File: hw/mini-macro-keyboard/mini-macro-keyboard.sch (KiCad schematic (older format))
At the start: 37 parts

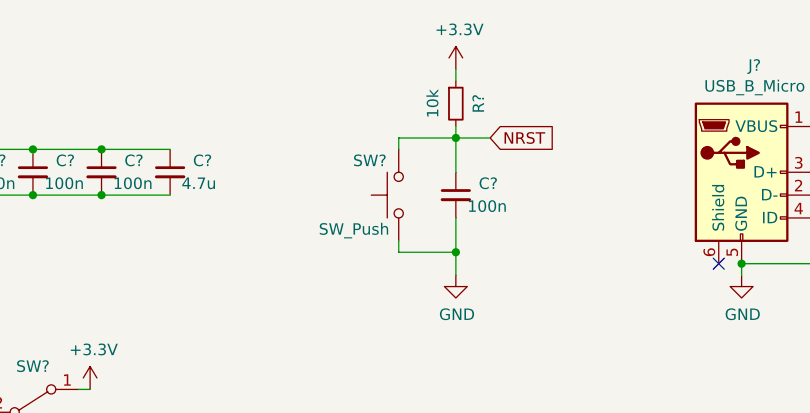
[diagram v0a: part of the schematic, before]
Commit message: style(hw): rename push switch
Signed-off-by: Ivan Kovalenko <s1ckretbox@gmail.com>
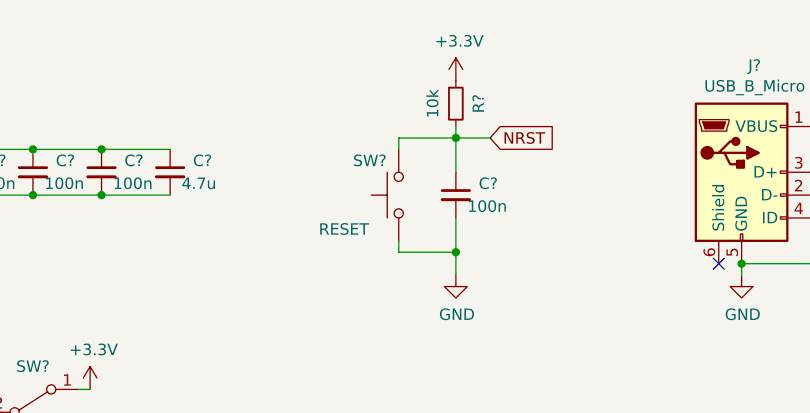
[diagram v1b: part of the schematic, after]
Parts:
- SW?: value SW_Push -> RESET
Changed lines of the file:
@@
 NRST
-Wire Wire Line
-	3750 800  3750 750
 Wire Wire Line
 	3750 1000 3750 1050
@@
 P 3500 1300
 F 0 "SW?" V 3650 1500 50  0000 R CNN
-F 1 "SW_Push" V 3350 1650 50  0000 R CNN
+F 1 "RESET" V 3350 1650 50  0000 R CNN
 F 2 "" H 3500 1500 50  0001 C CNN
 F 3 "~" H 3500 1500 50  0001 C CNN
@@
 L power:+3.3V #PWR?
 U 1 1 5FFB05C0
-P 3750 750
-F 0 "#PWR?" H 3750 600 50  0001 C CNN
-F 1 "+3.3V" H 3765 923 50  0000 C CNN
-F 2 "" H 3750 750 50  0001 C CNN
-F 3 "" H 3750 750 50  0001 C CNN
-	1    3750 750
-	1    0    0    -1
-$EndComp
+P 3750 800
+F 0 "#PWR?" H 3750 650 50  0001 C CNN
+F 1 "+3.3V" H 3765 973 50  0000 C CNN
+F 2 "" H 3750 800 50  0001 C CNN
+F 3 "" H 3750 800 50  0001 C CNN
+	1    3750 800
+	1    0    0    -1
+$EndComp

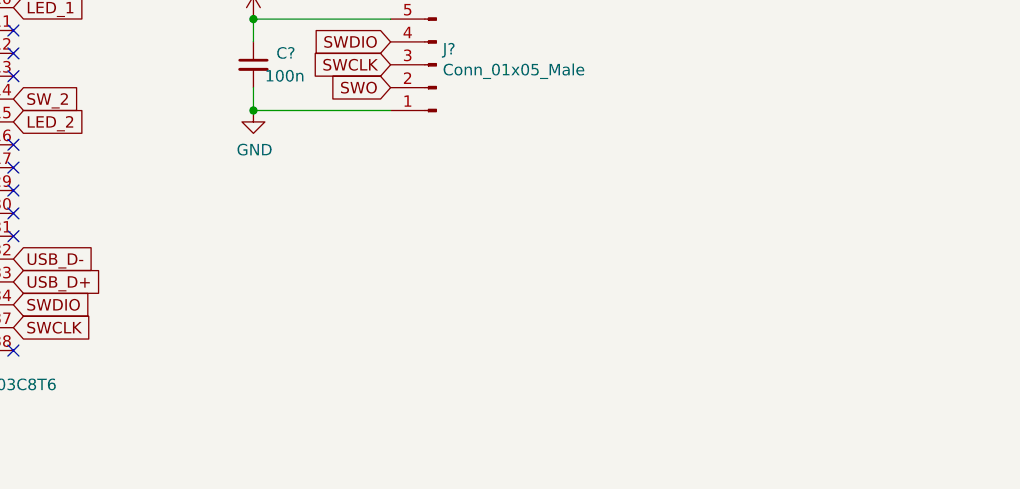
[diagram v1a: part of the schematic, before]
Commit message: feat(hw): add switches
Signed-off-by: Ivan Kovalenko <s1ckretbox@gmail.com>
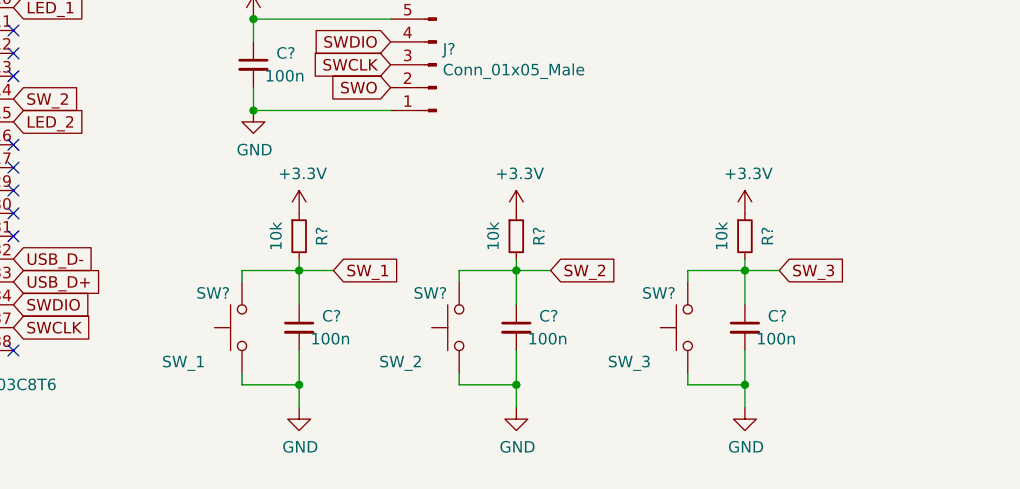
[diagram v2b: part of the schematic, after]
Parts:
- added C? (x3): 100n, symbol Device:C_Small
- added R? (x3): 10k, symbol Device:R_Small
- added SW?: SW_1, symbol Switch:SW_Push
- added SW?: SW_2, symbol Switch:SW_Push
- added SW?: SW_3, symbol Switch:SW_Push
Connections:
- net +3V3: now also R?.1, R?.1, R?.1
- net GND: now also C?.2, C?.2, C?.2, SW?.1, SW?.1, SW?.1
- net SW_1: now also C?.1, R?.2, SW?.2
- net SW_2: now also C?.1, R?.2, SW?.2
- net SW_3: now also C?.1, R?.2, SW?.2
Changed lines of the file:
@@
 	1    0    0    -1
 $EndComp
+$Comp
+L Device:C_Small C?
+U 1 1 5FFBA63C
+P 3750 7050
+F 0 "C?" H 3850 7100 50  0000 L CNN
+F 1 "100n" H 3800 7000 50  0000 L CNN
+F 2 "" H 3750 7050 50  0001 C CNN
+F 3 "~" H 3750 7050 50  0001 C CNN
+	1    3750 7050
+	1    0    0    -1
+$EndComp
+Wire Wire Line
+	3750 6750 3750 6800
+$Comp
+L power:GND #PWR?
+U 1 1 5FFBA643
+P 3750 7400
+F 0 "#PWR?" H 3750 7150 50  0001 C CNN
+F 1 "GND" H 3755 7227 50  0000 C CNN
+F 2 "" H 3750 7400 50  0001 C CNN
+F 3 "" H 3750 7400 50  0001 C CNN
+	1    3750 7400
+	1    0    0    -1
+$EndComp
+Wire Wire Line
+	3750 6950 3750 6800
+Connection ~ 3750 6800
+Wire Wire Line
+	3750 6800 3900 6800
+$Comp
+L Device:R_Small R?
+U 1 1 5FFBA64D
+P 3750 6650
+F 0 "R?" V 3850 6650 50  0000 C CNN
+F 1 "10k" V 3650 6650 50  0000 C CNN
+F 2 "" H 3750 6650 50  0001 C CNN
+F 3 "~" H 3750 6650 50  0001 C CNN
+	1    3750 6650
+	1    0    0    -1
+$EndComp
+$Comp
+L Switch:SW_Push SW?
+U 1 1 5FFBA653
+P 3500 7050
+F 0 "SW?" V 3650 7250 50  0000 R CNN
+F 1 "SW_1" V 3350 7400 50  0000 R CNN
+F 2 "" H 3500 7250 50  0001 C CNN
+F 3 "~" H 3500 7250 50  0001 C CNN
+	1    3500 7050
+	0    -1   -1   0
+$EndComp
+Wire Wire Line
+	3750 7150 3750 7300
+Wire Wire Line
+	3750 6800 3500 6800
+Wire Wire Line
+	3500 6800 3500 6850
+Wire Wire Line
+	3500 7250 3500 7300
+Wire Wire Line
+	3500 7300 3750 7300
+Connection ~ 3750 7300
+Wire Wire Line
+	3750 7300 3750 7400
+$Comp
+L power:+3.3V #PWR?
+U 1 1 5FFBA660
+P 3750 6550
+F 0 "#PWR?" H 3750 6400 50  0001 C CNN
+F 1 "+3.3V" H 3765 6723 50  0000 C CNN
+F 2 "" H 3750 6550 50  0001 C CNN
+F 3 "" H 3750 6550 50  0001 C CNN
+	1    3750 6550
+	1    0    0    -1
+$EndComp
+Text GLabel 3900 6800 2    50   Input ~ 0
+SW_1
+$Comp
+L Device:C_Small C?
+U 1 1 5FFBFAEB
+P 4700 7050
+F 0 "C?" H 4800 7100 50  0000 L CNN
+F 1 "100n" H 4750 7000 50  0000 L CNN
+F 2 "" H 4700 7050 50  0001 C CNN
+F 3 "~" H 4700 7050 50  0001 C CNN
+	1    4700 7050
+	1    0    0    -1
+$EndComp
+Wire Wire Line
+	4700 6750 4700 6800
+$Comp
+L power:GND #PWR?
+U 1 1 5FFBFAF2
+P 4700 7400
+F 0 "#PWR?" H 4700 7150 50  0001 C CNN
+F 1 "GND" H 4705 7227 50  0000 C CNN
+F 2 "" H 4700 7400 50  0001 C CNN
+F 3 "" H 4700 7400 50  0001 C CNN
+	1    4700 7400
+	1    0    0    -1
+$EndComp
+Wire Wire Line
+	4700 6950 4700 6800
+Connection ~ 4700 6800
+Wire Wire Line
+	4700 6800 4850 6800
+$Comp
+L Device:R_Small R?
+U 1 1 5FFBFAFB
+P 4700 6650
+F 0 "R?" V 4800 6650 50  0000 C CNN
+F 1 "10k" V 4600 6650 50  0000 C CNN
+F 2 "" H 4700 6650 50  0001 C CNN
+F 3 "~" H 4700 6650 50  0001 C CNN
+	1    4700 6650
+	1    0    0    -1
+$EndComp
+$Comp
+L Switch:SW_Push SW?
+U 1 1 5FFBFB01
+P 4450 7050
+F 0 "SW?" V 4600 7250 50  0000 R CNN
+F 1 "SW_2" V 4300 7400 50  0000 R CNN
+F 2 "" H 4450 7250 50  0001 C CNN
+F 3 "~" H 4450 7250 50  0001 C CNN
+	1    4450 7050
+	0    -1   -1   0
+$EndComp
+Wire Wire Line
+	4700 7150 4700 7300
+Wire Wire Line
+	4700 6800 4450 6800
+Wire Wire Line
+	4450 6800 4450 6850
+Wire Wire Line
+	4450 7250 4450 7300
+Wire Wire Line
+	4450 7300 4700 7300
+Connection ~ 4700 7300
+Wire Wire Line
+	4700 7300 4700 7400
+$Comp
+L power:+3.3V #PWR?
+U 1 1 5FFBFB0E
+P 4700 6550
+F 0 "#PWR?" H 4700 6400 50  0001 C CNN
+F 1 "+3.3V" H 4715 6723 50  0000 C CNN
+F 2 "" H 4700 6550 50  0001 C CNN
+F 3 "" H 4700 6550 50  0001 C CNN
+	1    4700 6550
+	1    0    0    -1
+$EndComp
+$Comp
+L Device:C_Small C?
+U 1 1 5FFC23D1
+P 5700 7050
+F 0 "C?" H 5800 7100 50  0000 L CNN
+F 1 "100n" H 5750 7000 50  0000 L CNN
+F 2 "" H 5700 7050 50  0001 C CNN
+F 3 "~" H 5700 7050 50  0001 C CNN
+	1    5700 7050
+	1    0    0    -1
+$EndComp
+Wire Wire Line
+	5700 6750 5700 6800
+$Comp
+L power:GND #PWR?
+U 1 1 5FFC23D8
+P 5700 7400
+F 0 "#PWR?" H 5700 7150 50  0001 C CNN
+F 1 "GND" H 5705 7227 50  0000 C CNN
+F 2 "" H 5700 7400 50  0001 C CNN
+F 3 "" H 5700 7400 50  0001 C CNN
+	1    5700 7400
+	1    0    0    -1
+$EndComp
+Wire Wire Line
+	5700 6950 5700 6800
+Connection ~ 5700 6800
+Wire Wire Line
+	5700 6800 5850 6800
+$Comp
+L Device:R_Small R?
+U 1 1 5FFC23E1
+P 5700 6650
+F 0 "R?" V 5800 6650 50  0000 C CNN
+F 1 "10k" V 5600 6650 50  0000 C CNN
+F 2 "" H 5700 6650 50  0001 C CNN
+F 3 "~" H 5700 6650 50  0001 C CNN
+	1    5700 6650
+	1    0    0    -1
+$EndComp
+$Comp
+L Switch:SW_Push SW?
+U 1 1 5FFC23E7
+P 5450 7050
+F 0 "SW?" V 5600 7250 50  0000 R CNN
+F 1 "SW_3" V 5300 7400 50  0000 R CNN
+F 2 "" H 5450 7250 50  0001 C CNN
+F 3 "~" H 5450 7250 50  0001 C CNN
+	1    5450 7050
+	0    -1   -1   0
+$EndComp
+Wire Wire Line
+	5700 7150 5700 7300
+Wire Wire Line
+	5700 6800 5450 6800
+Wire Wire Line
+	5450 6800 5450 6850
+Wire Wire Line
+	5450 7250 5450 7300
+Wire Wire Line
+	5450 7300 5700 7300
+Connection ~ 5700 7300
+Wire Wire Line
+	5700 7300 5700 7400
+$Comp
+L power:+3.3V #PWR?
+U 1 1 5FFC23F4
+P 5700 6550
+F 0 "#PWR?" H 5700 6400 50  0001 C CNN
+F 1 "+3.3V" H 5715 6723 50  0000 C CNN
+F 2 "" H 5700 6550 50  0001 C CNN
+F 3 "" H 5700 6550 50  0001 C CNN
+	1    5700 6550
+	1    0    0    -1
+$EndComp
+Text GLabel 4850 6800 2    50   Input ~ 0
+SW_2
+Text GLabel 5850 6800 2    50   Input ~ 0
+SW_3
 $EndSCHEMATC

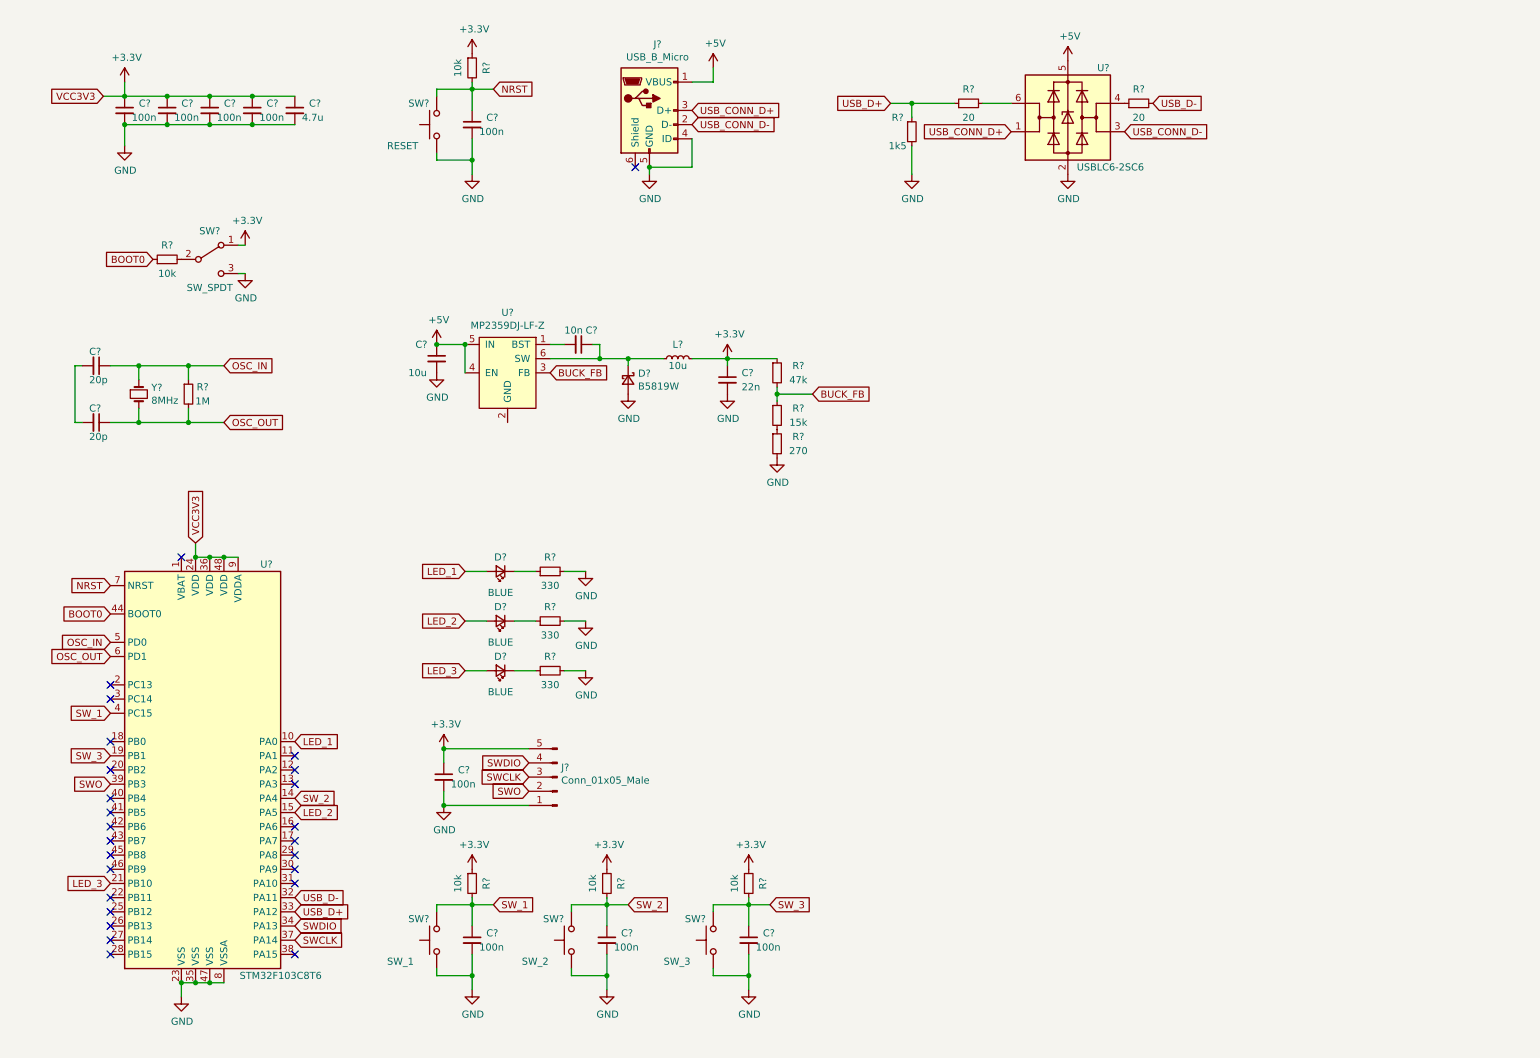
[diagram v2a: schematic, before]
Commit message: style(hw): devide schematic into sections
Signed-off-by: Ivan Kovalenko <s1ckretbox@gmail.com>
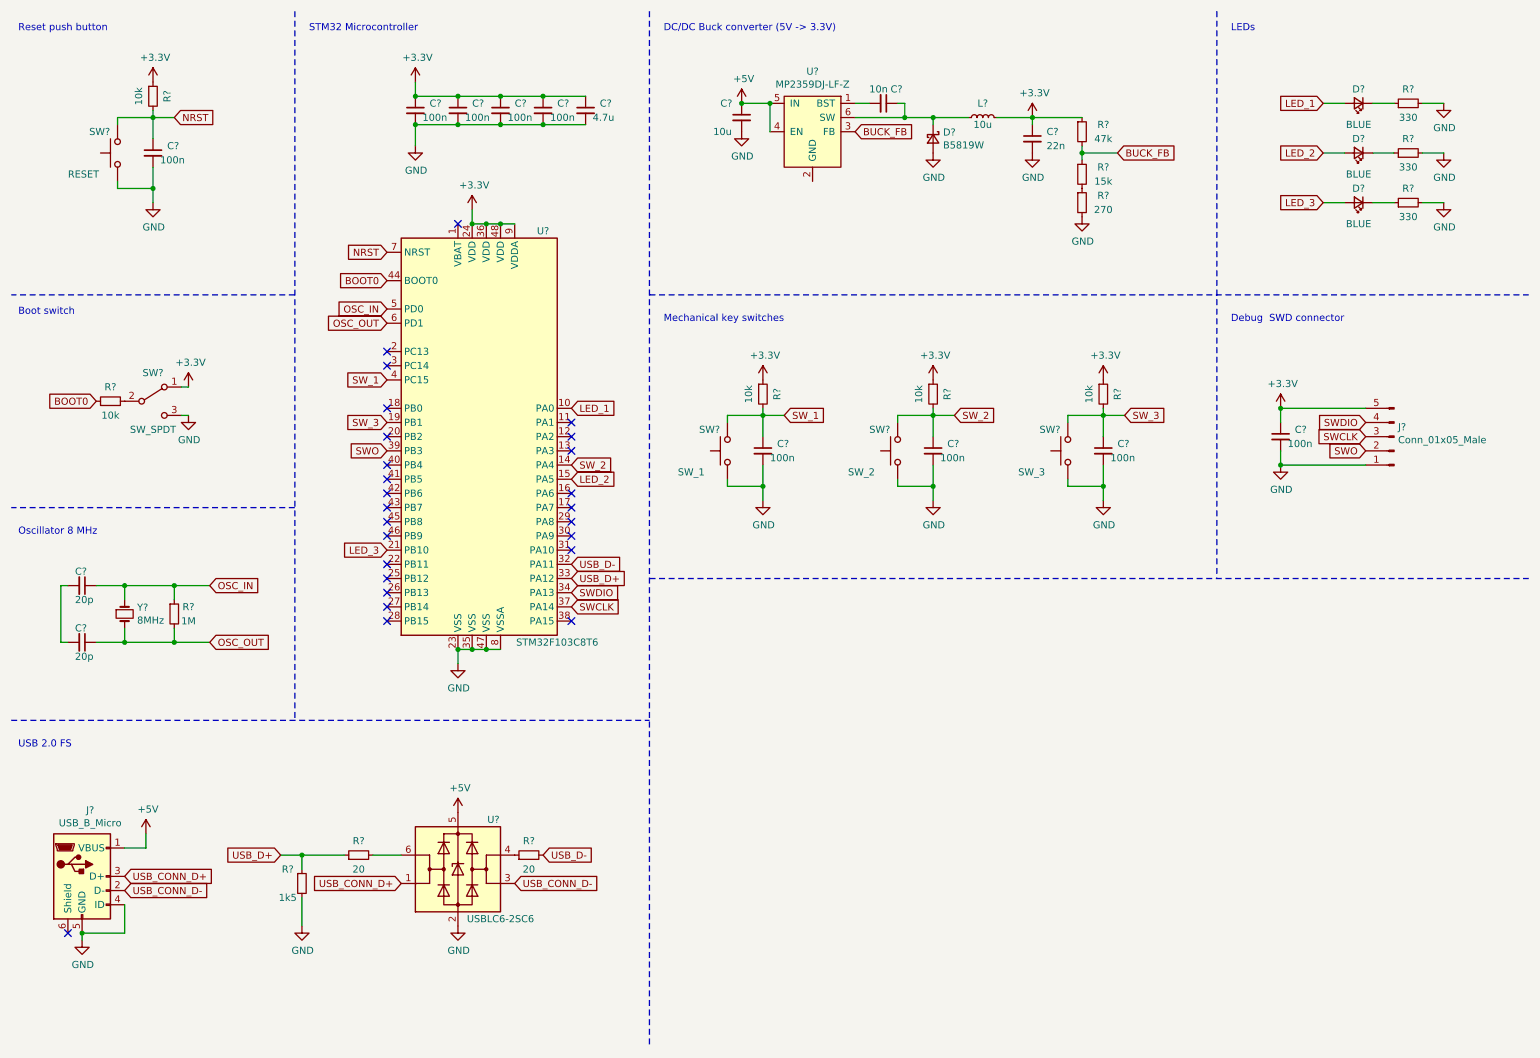
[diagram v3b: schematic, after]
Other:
- note added: "Boot switch"
- note added: "DC/DC Buck converter (5V -> 3.3V)"
- note added: "Debug SWD connector"
- note added: "LEDs\n"
- note added: "Mechanical key switches"
- note added: "Oscillator 8 MHz"
- note added: "Reset push button"
- note added: "STM32 Microcontroller\n"
- note added: "USB 2.0 FS"
- moved on the sheet: C?, D?, J?, L?, R?, SW?, U?, Y?

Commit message: feat(hw): annotate schematic
Signed-off-by: Ivan Kovalenko <s1ckretbox@gmail.com>
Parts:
- gave numbers to parts that had none: 46
